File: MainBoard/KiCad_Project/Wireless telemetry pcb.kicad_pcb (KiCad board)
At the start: 2 copper layers, 38.9 x 93.2 mm, 24 parts, among them J1 Conn_02x10_Counter_Clockwise, J2 Conn_02x06_Counter_Clockwise, J3 Conn_01x02_Male, Q1 BSS138, Q2 BSS138, SW1 SW_Push, U1 LD1117V33, U2 ControllerBoardV1

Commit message: Finished MainBoard
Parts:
- removed Q1, Q2: BSS138, digikey-footprints:SOT-23-3
- removed R3, R5, R6: 10k, Resistor_SMD:R_0603_1608Metric_Pad1.05x0.95mm_HandSolder
- removed R4: 1k, Resistor_SMD:R_0603_1608Metric_Pad1.05x0.95mm_HandSolder
- removed REF** (x3): MountingHole_2.2mm_M2, MountingHole:MountingHole_2.2mm_M2
- removed SW1: SW_Push, Lukas_Library:PTS636 SK25F SMTR LFS
- J1: value Conn_02x10_Counter_Clockwise -> XBEE
- J2: value Conn_02x06_Counter_Clockwise -> Molex MX120
- J3: value Conn_01x02_Male -> PWR HDR
- R1: value 1k -> 220
- R2: value 10k -> 220
- U1: value LD1117V33 -> NCV1117ST33
- U2: value ControllerBoardV1 -> ControllerBoardV2; footprint Lukas_Library:ControlBoardV1.0 -> Lukas_Library:Breadboard_Center_32pin
- moved R2 22.4 mm to (135.4, 42.5), turned to 90 degrees
- moved D2 10.3 mm to (103.4, 41.3), turned to 270 degrees
- moved U1 9.40 mm to (119.4, 62.2), turned to 270 degrees
- moved R1 5.93 mm to (105.7, 41.3), turned to 90 degrees
- moved D3 2.30 mm to (137.9, 42.5)
- moved C3 2.05 mm to (107.2, 33.3)
- moved U2 0.18 mm to (109.3, 59.8)
- turned J3 to 0 degrees
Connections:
- C3 pad 1: GND -> Vcc3.3V
- C3 pad 2: Vcc3.3V -> GND
- J1 pad 11: Net-(J1-Pad11) -> (no net)
- J1 pad 12: Net-(J1-Pad12) -> (no net)
- J1 pad 13: Net-(J1-Pad13) -> (no net)
- J1 pad 14: Net-(J1-Pad14) -> (no net)
- J1 pad 15: Associate\DIO5\AD5 -> ASSOC
- J1 pad 16: Net-(J1-Pad16) -> (no net)
- J1 pad 17: Net-(J1-Pad17) -> (no net)
- J1 pad 18: Net-(J1-Pad18) -> (no net)
- J1 pad 19: Net-(J1-Pad19) -> (no net)
- J1 pad 2: DOUT -> OUT
- J1 pad 20: AD0\DIO0\CommissioningPushbutton -> (no net)
- J1 pad 3: DIN -> IN
- J1 pad 4: Net-(J1-Pad4) -> (no net)
- J1 pad 5: Net-(J1-Pad5) -> (no net)
- J1 pad 6: Net-(J1-Pad6) -> (no net)
- J1 pad 7: Net-(J1-Pad7) -> (no net)
- J1 pad 8: Net-(J1-Pad8) -> (no net)
- J1 pad 9: Net-(J1-Pad9) -> (no net)
- J2 pad 10: Net-(J2-Pad10) -> (no net)
- J2 pad 11: Net-(J2-Pad11) -> CANH
- J2 pad 12: Net-(J2-Pad12) -> CANL
- J2 pad 3: Net-(J2-Pad3) -> (no net)
- J2 pad 4: Net-(J2-Pad4) -> (no net)
- J2 pad 5: Net-(J2-Pad5) -> (no net)
- J2 pad 6: Net-(J2-Pad6) -> (no net)
- J2 pad 7: Net-(J2-Pad7) -> (no net)
- J2 pad 8: Net-(J2-Pad8) -> (no net)
- J2 pad 9: Net-(J2-Pad9) -> (no net)
- J3 pad 1: Net-(J2-Pad1) -> +12V
- J3 pad 2: +12V -> Net-(J2-Pad1)
- R1 pad 1: Vcc3.3V -> Net-(D2-Pad2)
- R1 pad 2: Net-(D2-Pad2) -> Vcc3.3V
- R2 pad 1: Vcc3.3V -> Net-(D3-Pad2)
- R2 pad 2: DOUT -> ASSOC
- U2 pad 10: Net-(U2-Pad10) -> (no net)
- U2 pad 11: Net-(U2-Pad11) -> (no net)
- U2 pad 12: Net-(U2-Pad12) -> (no net)
- U2 pad 13: Net-(U2-Pad13) -> (no net)
- U2 pad 14: Net-(U2-Pad14) -> (no net)
- U2 pad 15: Net-(U2-Pad15) -> (no net)
- U2 pad 16: Net-(U2-Pad16) -> GND
- U2 pad 17: Net-(J2-Pad3) -> CANL
- U2 pad 18: Net-(J2-Pad4) -> CANH
- U2 pad 19: Net-(U2-Pad19) -> (no net)
- U2 pad 20: Vcc5V -> (no net)
- U2 pad 21: Net-(U2-Pad21) -> (no net)
- U2 pad 22: Net-(U2-Pad22) -> OUT
- U2 pad 23: Net-(U2-Pad23) -> IN
- U2 pad 24: Net-(U2-Pad24) -> (no net)
- U2 pad 25: OUT -> (no net)
- U2 pad 26: IN -> (no net)
- U2 pad 27: Net-(U2-Pad27) -> (no net)
- U2 pad 28: Net-(U2-Pad28) -> (no net)
- U2 pad 29: Net-(U2-Pad29) -> (no net)
- U2 pad 3: Net-(U2-Pad3) -> (no net)
- U2 pad 30: Net-(U2-Pad30) -> (no net)
- U2 pad 31: Net-(U2-Pad31) -> (no net)
- U2 pad 4: Net-(U2-Pad4) -> (no net)
- U2 pad 5: Net-(U2-Pad5) -> (no net)
- U2 pad 6: Net-(U2-Pad6) -> (no net)
- U2 pad 7: Net-(U2-Pad7) -> (no net)
- U2 pad 8: Net-(U2-Pad8) -> (no net)
- U2 pad 9: Net-(U2-Pad9) -> (no net)
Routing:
- net CANH: track 0.00 -> 50.7 mm
- net CANL: track 0.00 -> 50.6 mm
- net Net-(J2-Pad3): track 49.4 -> 0.00 mm
- net Net-(J2-Pad4): track 48.5 -> 0.00 mm
- net DOUT: track 33.0 -> 0.00 mm
- net DIN: track 29.7 -> 0.00 mm
- net OUT: track 24.7 -> 48.2 mm
- net Vcc3.3V: track 71.0 -> 50.2 mm
- net IN: track 29.4 -> 49.5 mm
- net Vcc5V: track 14.4 -> 0.00 mm
- net GND: track 0.00 -> 6.93 mm, vias 5 -> 6
- net +12V: track 45.9 -> 39.5 mm
- net AD0\DIO0\CommissioningPushbutton: track 5.92 -> 0.00 mm
- net Associate\DIO5\AD5: track 4.03 -> 0.00 mm
- net ASSOC: track 0.00 -> 3.74 mm
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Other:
- board text added: "12v"
- board text added: "GND"
- board text added: "H"
- board text added: "L"

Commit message: Finished MainBoard. Small routing improvements on ControlBoard
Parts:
- moved R1 1.27 mm to (105.7, 42.5)
- moved PWR 1.26 mm to (103.4, 42.5)
- renumbered D3 to ASSOC, D2 to PWR
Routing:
- net (no net): vias 2 -> 7
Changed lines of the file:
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@@
     (thickness 1.6)
     (drawings 15)
-    (tracks 64)
+    (tracks 70)
     (zones 0)
     (modules 14)
@@
     (mod_text_size 1 1)
     (mod_text_width 0.15)
-    (pad_size 3.8 2.2)
+    (pad_size 1.05 0.95)
     (pad_drill 0)
     (pad_to_mask_clearance 0.051)
@@
     (add_net "Net-(D2-Pad2)")
     (add_net "Net-(D3-Pad2)")
-    (add_net "Net-(J1-Pad11)")
-    (add_net "Net-(J1-Pad12)")
-    (add_net "Net-(J1-Pad13)")
-    (add_net "Net-(J1-Pad14)")
-    (add_net "Net-(J1-Pad16)")
-    (add_net "Net-(J1-Pad17)")
-    (add_net "Net-(J1-Pad18)")
-    (add_net "Net-(J1-Pad19)")
-    (add_net "Net-(J1-Pad20)")
-    (add_net "Net-(J1-Pad4)")
-    (add_net "Net-(J1-Pad5)")
-    (add_net "Net-(J1-Pad6)")
-    (add_net "Net-(J1-Pad7)")
-    (add_net "Net-(J1-Pad8)")
-    (add_net "Net-(J1-Pad9)")
     (add_net "Net-(J2-Pad1)")
-    (add_net "Net-(J2-Pad10)")
-    (add_net "Net-(J2-Pad3)")
-    (add_net "Net-(J2-Pad4)")
-    (add_net "Net-(J2-Pad5)")
-    (add_net "Net-(J2-Pad6)")
-    (add_net "Net-(J2-Pad7)")
-    (add_net "Net-(J2-Pad8)")
-    (add_net "Net-(J2-Pad9)")
-    (add_net "Net-(U2-Pad10)")
-    (add_net "Net-(U2-Pad11)")
-    (add_net "Net-(U2-Pad12)")
-    (add_net "Net-(U2-Pad13)")
-    (add_net "Net-(U2-Pad14)")
-    (add_net "Net-(U2-Pad15)")
-    (add_net "Net-(U2-Pad19)")
-    (add_net "Net-(U2-Pad20)")
-    (add_net "Net-(U2-Pad21)")
-    (add_net "Net-(U2-Pad24)")
-    (add_net "Net-(U2-Pad25)")
-    (add_net "Net-(U2-Pad26)")
-    (add_net "Net-(U2-Pad27)")
-    (add_net "Net-(U2-Pad28)")
-    (add_net "Net-(U2-Pad29)")
-    (add_net "Net-(U2-Pad3)")
-    (add_net "Net-(U2-Pad30)")
-    (add_net "Net-(U2-Pad31)")
-    (add_net "Net-(U2-Pad4)")
-    (add_net "Net-(U2-Pad5)")
-    (add_net "Net-(U2-Pad6)")
-    (add_net "Net-(U2-Pad7)")
-    (add_net "Net-(U2-Pad8)")
-    (add_net "Net-(U2-Pad9)")
     (add_net OUT)
     (add_net Vcc3.3V)
@@
   )
   (module Resistor_SMD:R_0603_1608Metric_Pad1.05x0.95mm_HandSolder (layer F.Cu)
-    (at 105.664 41.261 90)
+    (at 105.664 42.531 90)
     (descr "Resistor SMD 0603 (1608 Metric), square (rectangular) end terminal, IPC_7351 nominal with elongated pad for handsoldering. (Body size source: http://www.tortai-tech.com/upload/download/2011102023233369053.pdf), generated with kicad-footprint-generator")
     (tags "resistor handsolder")
@@
   )
   (module LED_SMD:LED_0603_1608Metric_Pad1.05x0.95mm_HandSolder (layer F.Cu)
-    (at 103.378 41.275 270)
+    (at 103.378 42.531 270)
     (descr "LED SMD 0603 (1608 Metric), square (rectangular) end terminal, IPC_7351 nominal, (Body size source: http://www.tortai-tech.com/upload/download/2011102023233369053.pdf), generated with kicad-footprint-generator")
     (tags "LED handsolder")
     (attr smd)
-    (fp_text reference D2 (at 0 1.3335 90) (layer F.SilkS)
+    (fp_text reference PWR (at 0 1.3335 90) (layer F.SilkS)
       (effects (font (size 1 1) (thickness 0.15)))
     )
@@
     (tags "LED handsolder")
     (attr smd)
-    (fp_text reference D3 (at 0 -1.524 90) (layer F.SilkS)
+    (fp_text reference ASSOC (at 0 -1.524 90) (layer F.SilkS)
       (effects (font (size 1 1) (thickness 0.15)))
     )
@@
   (via (at 102.7176 34.3916) (size 0.8) (drill 0.4) (layers F.Cu B.Cu) (net 0))
   (via (at 106.2736 31.0388) (size 0.8) (drill 0.4) (layers F.Cu B.Cu) (net 0))
-  (via (at 104.7496 62.3824) (size 0.8) (drill 0.4) (layers F.Cu B.Cu) (net 7))
+  (via (at 110.109 27.8384) (size 0.8) (drill 0.4) (layers F.Cu B.Cu) (net 0))
+  (via (at 114.427 24.2316) (size 0.8) (drill 0.4) (layers F.Cu B.Cu) (net 0))
+  (via (at 120.523 24.1808) (size 0.8) (drill 0.4) (layers F.Cu B.Cu) (net 0))
+  (via (at 126.873 24.1808) (size 0.8) (drill 0.4) (layers F.Cu B.Cu) (net 0))
+  (via (at 130.8608 27.7368) (size 0.8) (drill 0.4) (layers F.Cu B.Cu) (net 0))
   (segment (start 122.53 62.23) (end 116.23 62.23) (width 0.25) (layer F.Cu) (net 1))
   (segment (start 104.775 56.148) (end 107.188 53.735) (width 0.25) (layer F.Cu) (net 1))
@@
   (segment (start 107.188 34.879144) (end 107.188 34.135) (width 0.25) (layer F.Cu) (net 1))
   (segment (start 107.315 35.006144) (end 107.188 34.879144) (width 0.25) (layer F.Cu) (net 1))
-  (segment (start 105.664 40.386) (end 107.315 40.386) (width 0.25) (layer F.Cu) (net 1))
   (segment (start 107.315 40.386) (end 107.315 35.006144) (width 0.25) (layer F.Cu) (net 1))
-  (segment (start 107.315 53.608) (end 107.315 40.386) (width 0.25) (layer F.Cu) (net 1))
   (segment (start 106.831 61.087) (end 105.64571 59.90171) (width 0.25) (layer F.Cu) (net 1))
   (segment (start 113.8555 61.087) (end 106.831 61.087) (width 0.25) (layer F.Cu) (net 1))
@@
   (segment (start 104.267 89.324) (end 104.267 90.424) (width 0.25) (layer F.Cu) (net 2))
   (segment (start 104.902 70.461) (end 106.7435 72.3025) (width 0.25) (layer F.Cu) (net 2))
-  (segment (start 105.65 42.15) (end 105.664 42.136) (width 0.25) (layer F.Cu) (net 3))
-  (segment (start 103.378 42.15) (end 105.65 42.15) (width 0.25) (layer F.Cu) (net 3))
+  (segment (start 107.2896 41.656) (end 107.315 41.6306) (width 0.25) (layer F.Cu) (net 1))
+  (segment (start 105.664 41.656) (end 107.2896 41.656) (width 0.25) (layer F.Cu) (net 1))
+  (segment (start 107.315 41.6306) (end 107.315 40.386) (width 0.25) (layer F.Cu) (net 1))
+  (segment (start 107.315 53.608) (end 107.315 41.6306) (width 0.25) (layer F.Cu) (net 1))
+  (segment (start 103.378 43.406) (end 105.664 43.406) (width 0.25) (layer F.Cu) (net 3))
   (segment (start 135.957 43.406) (end 137.922 43.406) (width 0.25) (layer F.Cu) (net 4))
   (segment (start 135.382 43.406) (end 135.957 43.406) (width 0.25) (layer F.Cu) (net 4))
@@
   (segment (start 127.75649 70.60649) (end 131.445001 74.295001) (width 0.25) (layer F.Cu) (net 6))
   (segment (start 109.65 35.64) (end 110.8875 35.64) (width 0.25) (layer F.Cu) (net 6))
+  (via (at 104.7496 62.3824) (size 0.8) (drill 0.4) (layers F.Cu B.Cu) (net 7))
   (segment (start 109.46 59.93) (end 109.347 59.817) (width 0.25) (layer F.Cu) (net 7))
   (segment (start 116.23 59.93) (end 109.46 59.93) (width 0.25) (layer F.Cu) (net 7))

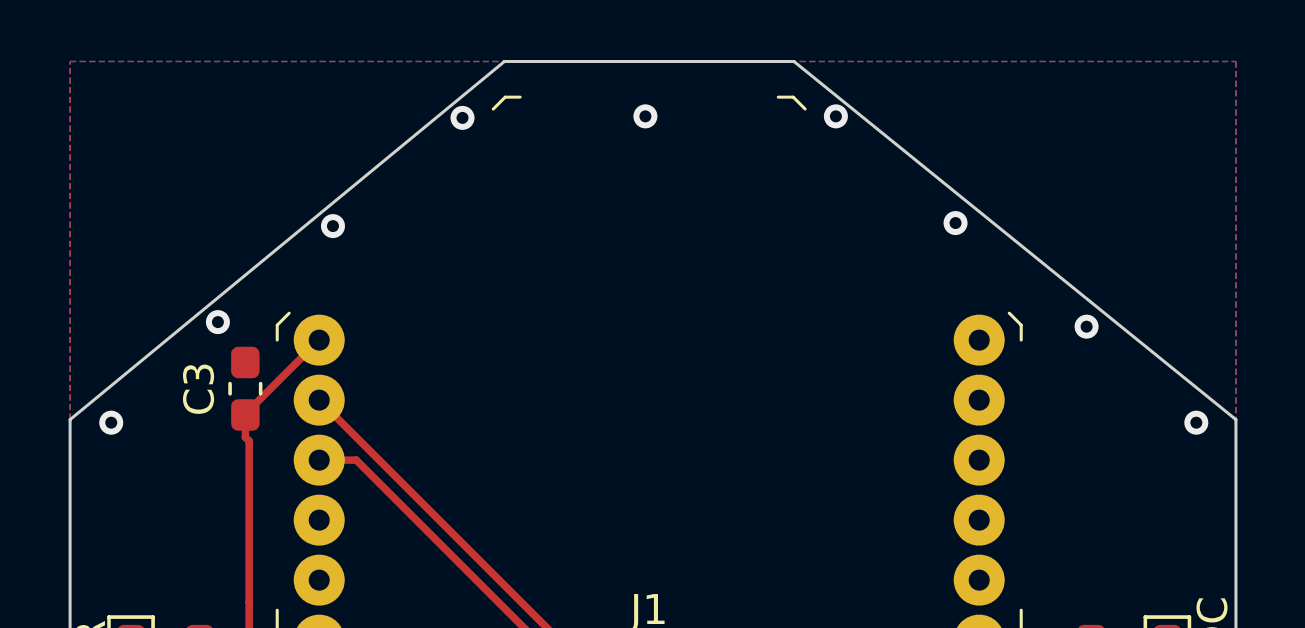
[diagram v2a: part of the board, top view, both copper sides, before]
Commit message: Fixed via net issue on mainboard
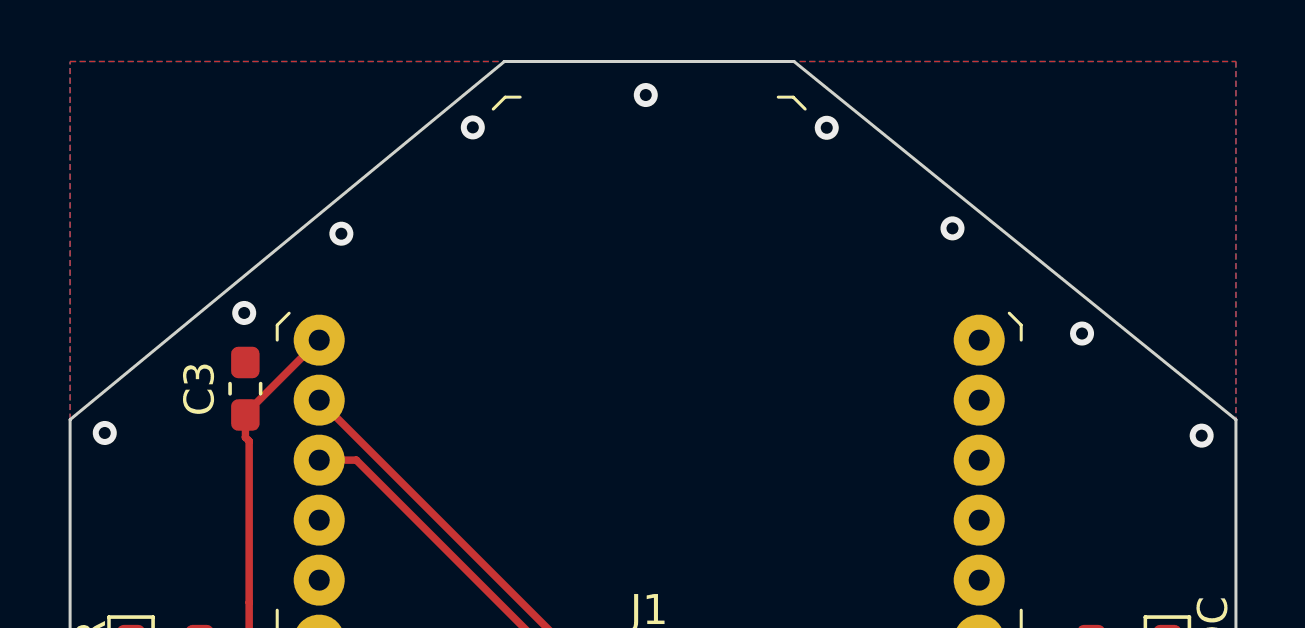
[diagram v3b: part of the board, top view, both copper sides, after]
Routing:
- net GND: vias 6 -> 13
- net (no net): vias 7 -> 0
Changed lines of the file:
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@@
     (effects (font (size 1 1) (thickness 0.15)))
   )
-  (via (at 102.7176 34.3916) (size 0.8) (drill 0.4) (layers F.Cu B.Cu) (net 0))
-  (via (at 106.2736 31.0388) (size 0.8) (drill 0.4) (layers F.Cu B.Cu) (net 0))
-  (via (at 110.109 27.8384) (size 0.8) (drill 0.4) (layers F.Cu B.Cu) (net 0))
-  (via (at 114.427 24.2316) (size 0.8) (drill 0.4) (layers F.Cu B.Cu) (net 0))
-  (via (at 120.523 24.1808) (size 0.8) (drill 0.4) (layers F.Cu B.Cu) (net 0))
-  (via (at 126.873 24.1808) (size 0.8) (drill 0.4) (layers F.Cu B.Cu) (net 0))
-  (via (at 130.8608 27.7368) (size 0.8) (drill 0.4) (layers F.Cu B.Cu) (net 0))
+  (via (at 102.5017 34.7345) (size 0.8) (drill 0.4) (layers F.Cu B.Cu) (net 7))
+  (via (at 107.1499 30.734) (size 0.8) (drill 0.4) (layers F.Cu B.Cu) (net 7))
+  (via (at 110.3884 28.0924) (size 0.8) (drill 0.4) (layers F.Cu B.Cu) (net 7))
+  (via (at 114.7699 24.5491) (size 0.8) (drill 0.4) (layers F.Cu B.Cu) (net 7))
+  (via (at 120.5357 23.4696) (size 0.8) (drill 0.4) (layers F.Cu B.Cu) (net 7))
+  (via (at 126.5682 24.5618) (size 0.8) (drill 0.4) (layers F.Cu B.Cu) (net 7))
+  (via (at 130.7592 27.9146) (size 0.8) (drill 0.4) (layers F.Cu B.Cu) (net 7))
   (segment (start 122.53 62.23) (end 116.23 62.23) (width 0.25) (layer F.Cu) (net 1))
   (segment (start 104.775 56.148) (end 107.188 53.735) (width 0.25) (layer F.Cu) (net 1))
@@
   (segment (start 105.64571 59.90171) (end 104.775 59.031) (width 0.25) (layer F.Cu) (net 1))
   (segment (start 116.23 62.23) (end 114.9985 62.23) (width 0.25) (layer F.Cu) (net 1))
+  (segment (start 107.2896 41.656) (end 107.315 41.6306) (width 0.25) (layer F.Cu) (net 1))
+  (segment (start 105.664 41.656) (end 107.2896 41.656) (width 0.25) (layer F.Cu) (net 1))
+  (segment (start 107.315 41.6306) (end 107.315 40.386) (width 0.25) (layer F.Cu) (net 1))
+  (segment (start 107.315 53.608) (end 107.315 41.6306) (width 0.25) (layer F.Cu) (net 1))
   (segment (start 105.777 69.586) (end 105.777 66.548) (width 0.25) (layer F.Cu) (net 2))
   (segment (start 104.902 70.461) (end 105.777 69.586) (width 0.25) (layer F.Cu) (net 2))
@@
   (segment (start 104.267 89.324) (end 104.267 90.424) (width 0.25) (layer F.Cu) (net 2))
   (segment (start 104.902 70.461) (end 106.7435 72.3025) (width 0.25) (layer F.Cu) (net 2))
-  (segment (start 107.2896 41.656) (end 107.315 41.6306) (width 0.25) (layer F.Cu) (net 1))
-  (segment (start 105.664 41.656) (end 107.2896 41.656) (width 0.25) (layer F.Cu) (net 1))
-  (segment (start 107.315 41.6306) (end 107.315 40.386) (width 0.25) (layer F.Cu) (net 1))
-  (segment (start 107.315 53.608) (end 107.315 41.6306) (width 0.25) (layer F.Cu) (net 1))
   (segment (start 103.378 43.406) (end 105.664 43.406) (width 0.25) (layer F.Cu) (net 3))
   (segment (start 135.957 43.406) (end 137.922 43.406) (width 0.25) (layer F.Cu) (net 4))
@@
   (segment (start 109.46 59.93) (end 109.347 59.817) (width 0.25) (layer F.Cu) (net 7))
   (segment (start 116.23 59.93) (end 109.46 59.93) (width 0.25) (layer F.Cu) (net 7))
-  (via (at 135.2296 31.1912) (size 0.8) (drill 0.4) (layers F.Cu B.Cu) (net 7))
-  (via (at 138.8872 34.3916) (size 0.8) (drill 0.4) (layers F.Cu B.Cu) (net 7))
+  (via (at 135.0772 31.4198) (size 0.8) (drill 0.4) (layers F.Cu B.Cu) (net 7))
+  (via (at 139.065 34.8234) (size 0.8) (drill 0.4) (layers F.Cu B.Cu) (net 7))
   (via (at 107.2388 57.7596) (size 0.8) (drill 0.4) (layers F.Cu B.Cu) (net 7))
   (via (at 102.616 66.4972) (size 0.8) (drill 0.4) (layers F.Cu B.Cu) (net 7))

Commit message: Telemetry and controllerboard update
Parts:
- U2: footprint Lukas_Library:Breadboard_Center_32pin -> Lukas_Library:ControlBoardV2.0
- renumbered PWR to D2, ASSOC to D3
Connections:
- J1 pad 11: (no net) -> Net-(J1-Pad11)
- J1 pad 12: (no net) -> Net-(J1-Pad12)
- J1 pad 13: (no net) -> Net-(J1-Pad13)
- J1 pad 14: (no net) -> Net-(J1-Pad14)
- J1 pad 16: (no net) -> Net-(J1-Pad16)
- J1 pad 17: (no net) -> Net-(J1-Pad17)
- J1 pad 18: (no net) -> Net-(J1-Pad18)
- J1 pad 19: (no net) -> Net-(J1-Pad19)
- J1 pad 20: (no net) -> Net-(J1-Pad20)
- J1 pad 4: (no net) -> Net-(J1-Pad4)
- J1 pad 5: (no net) -> Net-(J1-Pad5)
- J1 pad 6: (no net) -> Net-(J1-Pad6)
- J1 pad 7: (no net) -> Net-(J1-Pad7)
- J1 pad 8: (no net) -> Net-(J1-Pad8)
- J1 pad 9: (no net) -> Net-(J1-Pad9)
- J2 pad 10: (no net) -> Net-(J2-Pad10)
- J2 pad 3: (no net) -> Net-(J2-Pad3)
- J2 pad 4: (no net) -> Net-(J2-Pad4)
- J2 pad 5: (no net) -> Net-(J2-Pad5)
- J2 pad 6: (no net) -> Net-(J2-Pad6)
- J2 pad 7: (no net) -> Net-(J2-Pad7)
- J2 pad 8: (no net) -> Net-(J2-Pad8)
- J2 pad 9: (no net) -> Net-(J2-Pad9)
- U2 pad 10: (no net) -> Net-(U2-Pad10)
- U2 pad 11: (no net) -> Net-(U2-Pad11)
- U2 pad 12: (no net) -> Net-(U2-Pad12)
- U2 pad 13: (no net) -> Net-(U2-Pad13)
- U2 pad 14: (no net) -> Net-(U2-Pad14)
- U2 pad 15: (no net) -> Net-(U2-Pad15)
- U2 pad 19: (no net) -> Net-(U2-Pad19)
- U2 pad 20: (no net) -> Net-(U2-Pad20)
- U2 pad 21: (no net) -> Net-(U2-Pad21)
- U2 pad 24: (no net) -> Net-(U2-Pad24)
- U2 pad 25: (no net) -> Net-(U2-Pad25)
- U2 pad 26: (no net) -> Net-(U2-Pad26)
- U2 pad 27: (no net) -> Net-(U2-Pad27)
- U2 pad 28: (no net) -> Net-(U2-Pad28)
- U2 pad 29: (no net) -> Net-(U2-Pad29)
- U2 pad 3: (no net) -> Net-(U2-Pad3)
- U2 pad 30: (no net) -> Net-(U2-Pad30)
- U2 pad 31: (no net) -> Net-(U2-Pad31)
- U2 pad 4: (no net) -> Net-(U2-Pad4)
- U2 pad 5: (no net) -> Net-(U2-Pad5)
- U2 pad 6: (no net) -> Net-(U2-Pad6)
- U2 pad 7: (no net) -> Net-(U2-Pad7)
- U2 pad 8: (no net) -> Net-(U2-Pad8)
- U2 pad 9: (no net) -> Net-(U2-Pad9)
